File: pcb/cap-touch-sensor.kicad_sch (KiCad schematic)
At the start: 6 parts, among them U4 CAP1296-x-AIA

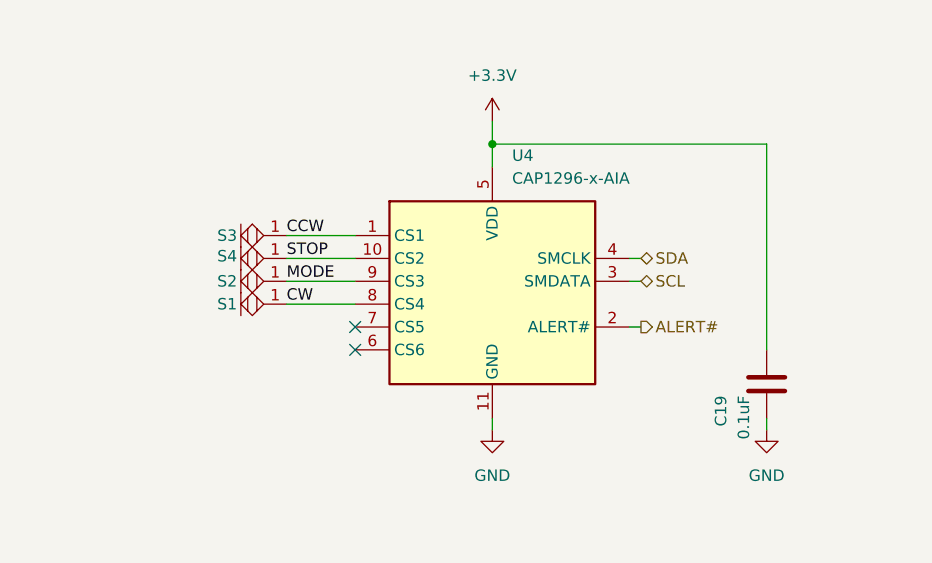
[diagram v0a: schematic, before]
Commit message: Revision E
- Resolve issues 1-11
- Add pdf of rev d schematic for easy comparison
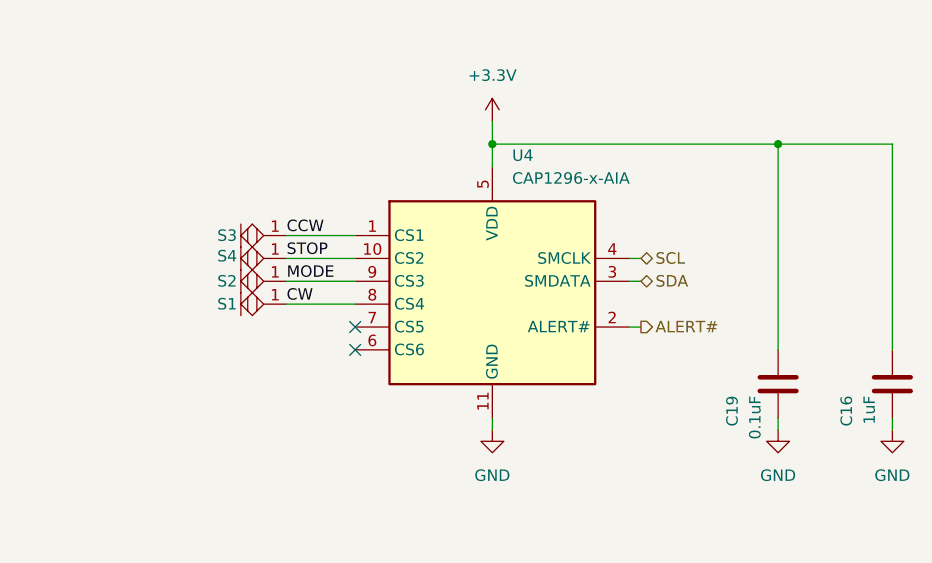
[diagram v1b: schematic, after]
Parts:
- added C16: 1uF, Capacitor_SMD:C_0603_1608Metric, symbol Device:C
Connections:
- net +3.3V: now also C16.1
- net GND: now also C16.2
- net SCL: now also U4.4 (SMCLK); no longer U4.3 (SMDATA)
- net SDA: now also U4.3 (SMDATA); no longer U4.4 (SMCLK)
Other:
- moved on the sheet: C19
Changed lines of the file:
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@@
+	)
+	(junction
+		(at 133.35 46.99)
+		(diameter 0)
+		(color 0 0 0 0)
 	)
 	(junction
@@
 	(wire
 		(pts
-			(xy 101.6 46.99) (xy 132.08 46.99)
+			(xy 101.6 46.99) (xy 133.35 46.99)
+		)
+		(stroke
+			(width 0)
+			(type default)
+		)
+	)
+	(wire
+		(pts
+			(xy 146.05 46.99) (xy 146.05 69.85)
 		)
 		(stroke
@@
 	(wire
 		(pts
-			(xy 132.08 46.99) (xy 132.08 69.85)
+			(xy 133.35 46.99) (xy 133.35 69.85)
 		)
 		(stroke
@@
 	(wire
 		(pts
+			(xy 133.35 46.99) (xy 146.05 46.99)
+		)
+		(stroke
+			(width 0)
+			(type default)
+		)
+	)
+	(wire
+		(pts
 			(xy 118.11 59.69) (xy 116.84 59.69)
 		)
@@
 	(wire
 		(pts
-			(xy 132.08 77.47) (xy 132.08 78.74)
+			(xy 133.35 77.47) (xy 133.35 78.74)
 		)
 		(stroke
@@
 		(pts
 			(xy 78.74 59.69) (xy 86.36 59.69)
+		)
+		(stroke
+			(width 0)
+			(type default)
+		)
+	)
+	(wire
+		(pts
+			(xy 146.05 77.47) (xy 146.05 78.74)
 		)
 		(stroke
@@
 	(hierarchical_label "SDA"
 		(shape bidirectional)
-		(at 118.11 59.69 0)
+		(at 118.11 62.23 0)
 		(fields_autoplaced yes)
 		(effects
@@
 	(hierarchical_label "SCL"
 		(shape bidirectional)
-		(at 118.11 62.23 0)
+		(at 118.11 59.69 0)
 		(fields_autoplaced yes)
 		(effects
@@
 	)
 	(symbol
+		(lib_id "power:GND")
+		(at 146.05 78.74 0)
+		(mirror y)
+		(unit 1)
+		(exclude_from_sim no)
+		(in_bom yes)
+		(on_board yes)
+		(dnp no)
+		(fields_autoplaced yes)
+		(property "Reference" "#PWR031"
+			(at 146.05 85.09 0)
+			(effects
+				(font
+					(size 1.27 1.27)
+				)
+				(hide yes)
+			)
+		)
+		(property "Value" "GND"
+			(at 146.05 83.82 0)
+			(effects
+				(font
+					(size 1.27 1.27)
+				)
+			)
+		)
+		(property "Footprint" ""
+			(at 146.05 78.74 0)
+			(effects
+				(font
+					(size 1.27 1.27)
+				)
+				(hide yes)
+			)
+		)
+		(property "Datasheet" ""
+			(at 146.05 78.74 0)
+			(effects
+				(font
+					(size 1.27 1.27)
+				)
+				(hide yes)
+			)
+		)
+		(property "Description" "Power symbol creates a global label with name \"GND\" , ground"
+			(at 146.05 78.74 0)
+			(effects
+				(font
+					(size 1.27 1.27)
+				)
+				(hide yes)
+			)
+		)
+		(pin "1"
+		)
+		(instances
+			(project "oe-commutator-controller"
+				(path "/f8e1d654-dc44-4fb2-953c-f5982945ff40/f9d22632-be45-4b30-a0f8-f307d3c7c772"
+					(reference "#PWR031")
+					(unit 1)
+				)
+			)
+		)
+	)
+	(symbol
 		(lib_id "Device:C")
-		(at 132.08 73.66 0)
+		(at 133.35 73.66 0)
 		(mirror y)
 		(unit 1)
@@
 		(dnp no)
 		(property "Reference" "C19"
-			(at 127 74.93 90)
+			(at 128.27 74.93 90)
 			(effects
 				(font
@@
 		)
 		(property "Value" "0.1uF"
-			(at 129.54 74.93 90)
+			(at 130.81 74.93 90)
 			(effects
 				(font
@@
 		)
 		(property "Footprint" "Capacitor_SMD:C_0402_1005Metric"
-			(at 131.1148 77.47 0)
+			(at 132.3848 77.47 0)
 			(effects
 				(font
@@
 		)
 		(property "Datasheet" "~"
-			(at 132.08 73.66 0)
+			(at 133.35 73.66 0)
 			(effects
 				(font
@@
 		)
 		(property "Description" "Unpolarized capacitor"
-			(at 132.08 73.66 0)
+			(at 133.35 73.66 0)
 			(effects
 				(font
@@
 				(path "/f8e1d654-dc44-4fb2-953c-f5982945ff40/f9d22632-be45-4b30-a0f8-f307d3c7c772"
 					(reference "C19")
+					(unit 1)
+				)
+			)
+		)
+	)
+	(symbol
+		(lib_id "Device:C")
+		(at 146.05 73.66 0)
+		(mirror y)
+		(unit 1)
+		(exclude_from_sim no)
+		(in_bom yes)
+		(on_board yes)
+		(dnp no)
+		(property "Reference" "C16"
+			(at 140.97 74.93 90)
+			(effects
+				(font
+					(size 1.27 1.27)
+				)
+				(justify right)
+			)
+		)
+		(property "Value" "1uF"
+			(at 143.51 74.93 90)
+			(effects
+				(font
+					(size 1.27 1.27)
+				)
+				(justify right)
+			)
+		)
+		(property "Footprint" "Capacitor_SMD:C_0603_1608Metric"
+			(at 145.0848 77.47 0)
+			(effects
+				(font
+					(size 1.27 1.27)
+				)
+				(hide yes)
+			)
+		)
+		(property "Datasheet" "~"
+			(at 146.05 73.66 0)
+			(effects
+				(font
+					(size 1.27 1.27)
+				)
+				(hide yes)
+			)
+		)
+		(property "Description" "Unpolarized capacitor"
+			(at 146.05 73.66 0)
+			(effects
+				(font
+					(size 1.27 1.27)
+				)
+				(hide yes)
+			)
+		)
+		(pin "1"
+		)
+		(pin "2"
+		)
+		(instances
+			(project "oe-commutator-controller"
+				(path "/f8e1d654-dc44-4fb2-953c-f5982945ff40/f9d22632-be45-4b30-a0f8-f307d3c7c772"
+					(reference "C16")
 					(unit 1)
 				)
@@
 	(symbol
 		(lib_id "power:GND")
-		(at 132.08 78.74 0)
+		(at 133.35 78.74 0)
 		(mirror y)
 		(unit 1)
@@
 		(fields_autoplaced yes)
 		(property "Reference" "#PWR037"
-			(at 132.08 85.09 0)
+			(at 133.35 85.09 0)
 			(effects
 				(font
@@
 		)
 		(property "Value" "GND"
-			(at 132.08 83.82 0)
+			(at 133.35 83.82 0)
 			(effects
 				(font
@@
 		)
 		(property "Footprint" ""
-			(at 132.08 78.74 0)
+			(at 133.35 78.74 0)
 			(effects
 				(font
@@
 		)
 		(property "Datasheet" ""
-			(at 132.08 78.74 0)
+			(at 133.35 78.74 0)
 			(effects
 				(font
@@
 		)
 		(property "Description" "Power symbol creates a global label with name \"GND\" , ground"
-			(at 132.08 78.74 0)
-			(effects
-				(font
+			(at 133.35 78.74 0)
+			(effects
+				(font

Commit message: Address schematic and PCB issues for Rev. E
- Some layout alternations
- Some schematic cleanup
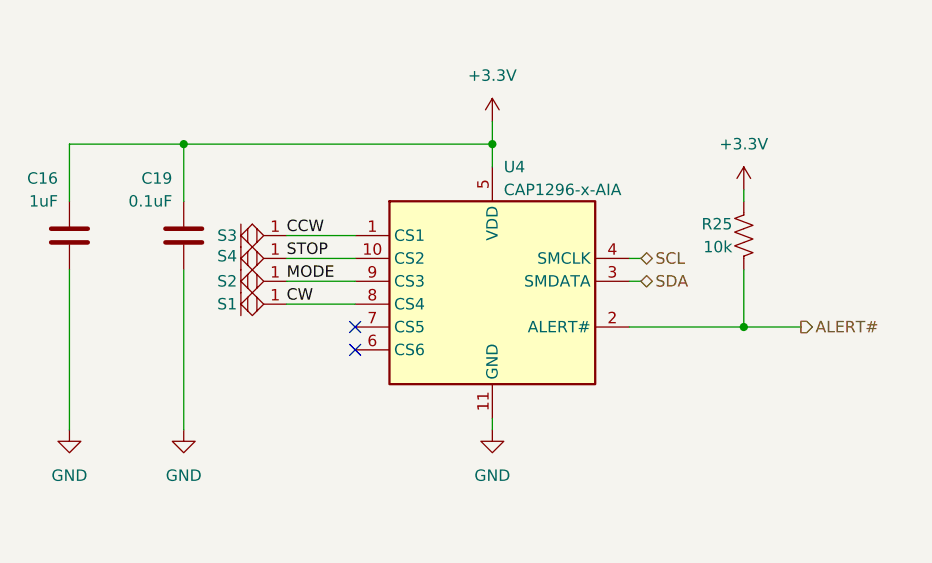
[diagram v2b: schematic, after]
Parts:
- added R25: 10k, Resistor_SMD:R_0603_1608Metric, symbol Device:R_US
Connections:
- net +3.3V: now also R25.1
- net ALERT#: now also R25.2
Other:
- moved on the sheet: C16, C19
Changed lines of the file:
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@@
 	(title_block
 		(title "Open Ephys Commutator Controller")
-		(rev "D")
+		(rev "E")
 		(company "Open Ephys, Inc.")
+		(comment 1 "Cris Sharp")
+		(comment 2 "Jonathan P. Newman")
 	)
 	(junction
-		(at 133.35 46.99)
+		(at 67.31 46.99)
+		(diameter 0)
+		(color 0 0 0 0)
+	)
+	(junction
+		(at 129.54 67.31)
 		(diameter 0)
 		(color 0 0 0 0)
@@
 	(wire
 		(pts
-			(xy 101.6 46.99) (xy 133.35 46.99)
-		)
-		(stroke
-			(width 0)
-			(type default)
-		)
-	)
-	(wire
-		(pts
-			(xy 146.05 46.99) (xy 146.05 69.85)
-		)
-		(stroke
-			(width 0)
-			(type default)
-		)
-	)
-	(wire
-		(pts
-			(xy 118.11 67.31) (xy 116.84 67.31)
+			(xy 67.31 46.99) (xy 101.6 46.99)
+		)
+		(stroke
+			(width 0)
+			(type default)
+		)
+	)
+	(wire
+		(pts
+			(xy 54.61 46.99) (xy 54.61 53.34)
+		)
+		(stroke
+			(width 0)
+			(type default)
+		)
+	)
+	(wire
+		(pts
+			(xy 135.89 67.31) (xy 129.54 67.31)
 		)
 		(stroke
@@
 	(wire
 		(pts
-			(xy 133.35 46.99) (xy 133.35 69.85)
+			(xy 67.31 46.99) (xy 67.31 53.34)
+		)
+		(stroke
+			(width 0)
+			(type default)
+		)
+	)
+	(wire
+		(pts
+			(xy 129.54 60.96) (xy 129.54 67.31)
 		)
 		(stroke
@@
 	(wire
 		(pts
+			(xy 129.54 52.07) (xy 129.54 53.34)
+		)
+		(stroke
+			(width 0)
+			(type default)
+		)
+	)
+	(wire
+		(pts
 			(xy 101.6 44.45) (xy 101.6 46.99)
 		)
@@
 	(wire
 		(pts
-			(xy 133.35 46.99) (xy 146.05 46.99)
+			(xy 67.31 46.99) (xy 54.61 46.99)
 		)
 		(stroke
@@
 	(wire
 		(pts
-			(xy 133.35 77.47) (xy 133.35 78.74)
+			(xy 67.31 60.96) (xy 67.31 78.74)
 		)
 		(stroke
@@
 	(wire
 		(pts
-			(xy 146.05 77.47) (xy 146.05 78.74)
+			(xy 54.61 60.96) (xy 54.61 78.74)
+		)
+		(stroke
+			(width 0)
+			(type default)
+		)
+	)
+	(wire
+		(pts
+			(xy 129.54 67.31) (xy 116.84 67.31)
 		)
 		(stroke
@@
 	(hierarchical_label "ALERT#"
 		(shape output)
-		(at 118.11 67.31 0)
+		(at 135.89 67.31 0)
 		(fields_autoplaced yes)
 		(effects
@@
 	(symbol
 		(lib_id "power:GND")
-		(at 146.05 78.74 0)
-		(mirror y)
+		(at 54.61 78.74 0)
 		(unit 1)
 		(exclude_from_sim no)
@@
 		(fields_autoplaced yes)
 		(property "Reference" "#PWR031"
-			(at 146.05 85.09 0)
+			(at 54.61 85.09 0)
 			(effects
 				(font
@@
 		)
 		(property "Value" "GND"
-			(at 146.05 83.82 0)
+			(at 54.61 83.82 0)
 			(effects
 				(font
@@
 		)
 		(property "Footprint" ""
-			(at 146.05 78.74 0)
+			(at 54.61 78.74 0)
 			(effects
 				(font
@@
 		)
 		(property "Datasheet" ""
-			(at 146.05 78.74 0)
+			(at 54.61 78.74 0)
 			(effects
 				(font
@@
 		)
 		(property "Description" "Power symbol creates a global label with name \"GND\" , ground"
-			(at 146.05 78.74 0)
+			(at 54.61 78.74 0)
 			(effects
 				(font
@@
 	)
 	(symbol
+		(lib_id "Device:R_US")
+		(at 129.54 57.15 0)
+		(mirror y)
+		(unit 1)
+		(exclude_from_sim no)
+		(in_bom yes)
+		(on_board yes)
+		(dnp no)
+		(property "Reference" "R25"
+			(at 128.27 55.88 0)
+			(effects
+				(font
+					(size 1.27 1.27)
+				)
+				(justify left)
+			)
+		)
+		(property "Value" "10k"
+			(at 128.27 58.42 0)
+			(effects
+				(font
+					(size 1.27 1.27)
+				)
+				(justify left)
+			)
+		)
+		(property "Footprint" "Resistor_SMD:R_0603_1608Metric"
+			(at 128.524 57.404 90)
+			(effects
+				(font
+					(size 1.27 1.27)
+				)
+				(hide yes)
+			)
+		)
+		(property "Datasheet" "~"
+			(at 129.54 57.15 0)
+			(effects
+				(font
+					(size 1.27 1.27)
+				)
+				(hide yes)
+			)
+		)
+		(property "Description" "Resistor, US symbol"
+			(at 129.54 57.15 0)
+			(effects
+				(font
+					(size 1.27 1.27)
+				)
+				(hide yes)
+			)
+		)
+		(pin "1"
+		)
+		(pin "2"
+		)
+		(instances
+			(project "oe-commutator-controller"
+				(path "/f8e1d654-dc44-4fb2-953c-f5982945ff40/f9d22632-be45-4b30-a0f8-f307d3c7c772"
+					(reference "R25")
+					(unit 1)
+				)
+			)
+		)
+	)
+	(symbol
 		(lib_id "Device:C")
-		(at 133.35 73.66 0)
-		(mirror y)
+		(at 67.31 57.15 0)
 		(unit 1)
 		(exclude_from_sim no)
@@
 		(dnp no)
 		(property "Reference" "C19"
-			(at 128.27 74.93 90)
+			(at 66.04 50.8 0)
 			(effects
 				(font
@@
 		)
 		(property "Value" "0.1uF"
-			(at 130.81 74.93 90)
+			(at 66.04 53.34 0)
 			(effects
 				(font
@@
 		)
 		(property "Footprint" "Capacitor_SMD:C_0402_1005Metric"
-			(at 132.3848 77.47 0)
+			(at 68.2752 60.96 0)
 			(effects
 				(font
@@
 		)
 		(property "Datasheet" "~"
-			(at 133.35 73.66 0)
+			(at 67.31 57.15 0)
 			(effects
 				(font
@@
 		)
 		(property "Description" "Unpolarized capacitor"
-			(at 133.35 73.66 0)
+			(at 67.31 57.15 0)
 			(effects
 				(font
@@
 	)
 	(symbol
+		(lib_id "power:+3.3V")
+		(at 129.54 52.07 0)
+		(unit 1)
+		(exclude_from_sim no)
+		(in_bom yes)
+		(on_board yes)
+		(dnp no)
+		(fields_autoplaced yes)
+		(property "Reference" "#PWR029"
+			(at 129.54 55.88 0)
+			(effects
+				(font
+					(size 1.27 1.27)
+				)
+				(hide yes)
+			)
+		)
+		(property "Value" "+3.3V"
+			(at 129.54 46.99 0)
+			(effects
+				(font
+					(size 1.27 1.27)
+				)
+			)
+		)
+		(property "Footprint" ""
+			(at 129.54 52.07 0)
+			(effects
+				(font
+					(size 1.27 1.27)
+				)
+				(hide yes)
+			)
+		)
+		(property "Datasheet" ""
+			(at 129.54 52.07 0)
+			(effects
+				(font
+					(size 1.27 1.27)
+				)
+				(hide yes)
+			)
+		)
+		(property "Description" "Power symbol creates a global label with name \"+3.3V\""
+			(at 129.54 52.07 0)
+			(effects
+				(font
+					(size 1.27 1.27)
+				)
+				(hide yes)
+			)
+		)
+		(pin "1"
+		)
+		(instances
+			(project "oe-commutator-controller"
+				(path "/f8e1d654-dc44-4fb2-953c-f5982945ff40/f9d22632-be45-4b30-a0f8-f307d3c7c772"
+					(reference "#PWR029")
+					(unit 1)
+				)
+			)
+		)
+	)
+	(symbol
 		(lib_id "Device:C")
-		(at 146.05 73.66 0)
-		(mirror y)
+		(at 54.61 57.15 0)
 		(unit 1)
 		(exclude_from_sim no)
@@
 		(dnp no)
 		(property "Reference" "C16"
-			(at 140.97 74.93 90)
+			(at 53.34 50.8 0)
 			(effects
 				(font
@@
 		)
 		(property "Value" "1uF"
-			(at 143.51 74.93 90)
+			(at 53.34 53.34 0)
 			(effects
 				(font
@@
 		)
 		(property "Footprint" "Capacitor_SMD:C_0603_1608Metric"
-			(at 145.0848 77.47 0)
+			(at 55.5752 60.96 0)
 			(effects
 				(font
@@
 		)
 		(property "Datasheet" "~"
-			(at 146.05 73.66 0)
+			(at 54.61 57.15 0)
 			(effects
 				(font
@@
 		)
 		(property "Description" "Unpolarized capacitor"
-			(at 146.05 73.66 0)
+			(at 54.61 57.15 0)
 			(effects
 				(font
@@
 	(symbol
 		(lib_id "power:GND")
-		(at 133.35 78.74 0)
-		(mirror y)
+		(at 67.31 78.74 0)
 		(unit 1)
 		(exclude_from_sim no)
@@
 		(fields_autoplaced yes)
 		(property "Reference" "#PWR037"
-			(at 133.35 85.09 0)
+			(at 67.31 85.09 0)
 			(effects
 				(font
@@
 		)
 		(property "Value" "GND"
-			(at 133.35 83.82 0)
+			(at 67.31 83.82 0)
 			(effects
 				(font
@@
 		)
 		(property "Footprint" ""
-			(at 133.35 78.74 0)
+			(at 67.31 78.74 0)
 			(effects
 				(font
@@
 		)
 		(property "Datasheet" ""
-			(at 133.35 78.74 0)
+			(at 67.31 78.74 0)
 			(effects
 				(font
@@
 		)
 		(property "Description" "Power symbol creates a global label with name \"GND\" , ground"
-			(at 133.35 78.74 0)
+			(at 67.31 78.74 0)
 			(effects
 				(font
@@
 		(on_board yes)
 		(dnp no)
-		(fields_autoplaced yes)
 		(property "Reference" "U4"
-			(at 103.7941 48.26 0)
+			(at 102.87 49.53 0)
 			(effects
 				(font
@@
 		)
 		(property "Value" "CAP1296-x-AIA"
-			(at 103.7941 50.8 0)
-			(effects
-				(font
+			(at 102.87 52.07 0)
+			(effects
+				(font

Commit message: Revision F Edits
- Reduce base capacitance
  - Reduce infill {width, gap}: {0.35, 1} -> {0.2, 1.2}
    - Equivalent to: 45.1% -> 26.5%
  - Entirely remove copper on 3rd (in2.Cu) layer
  - Reduce via count
- export rev e schematic to pdf
- put pdfs into manufacturing folder
- Fix 6mm tactile switch footprint
- Put gold under logo
- Increment schematic, pcb, and silkscreen revision to F
- Add labels to debug header
- Add 10k pull-up to tmc2130 enable pin
- Convert all symbols & footprints library aliases from "oe" to "open-ephys"
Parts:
- S1, S2, S3, S4: footprint oe:Touch_Center_2mm -> open-ephys:Touch_Center_2mm; symbol oe:TOUCH -> open-ephys:TOUCH; now left out of the parts list
- U4: symbol oe:CAP1296-x-AIA -> open-ephys:CAP1296-x-AIA
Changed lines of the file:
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@@
 	)
 	(symbol
-		(lib_id "oe:TOUCH")
+		(lib_id "open-ephys:TOUCH")
 		(at 76.2 59.69 90)
 		(mirror x)
 		(unit 1)
 		(exclude_from_sim no)
-		(in_bom yes)
+		(in_bom no)
 		(on_board yes)
 		(dnp no)
@@
 			)
 		)
-		(property "Footprint" "oe:Touch_Center_2mm"
+		(property "Footprint" "open-ephys:Touch_Center_2mm"
 			(at 76.2 59.69 0)
 			(effects
@@
 			)
 		)
-		(property "Description" ""
+		(property "Description" "Printed capactitive touch sensor"
 			(at 76.2 59.69 0)
 			(effects
@@
 	)
 	(symbol
-		(lib_id "oe:TOUCH")
+		(lib_id "open-ephys:TOUCH")
 		(at 76.2 62.23 90)
 		(mirror x)
 		(unit 1)
 		(exclude_from_sim no)
-		(in_bom yes)
+		(in_bom no)
 		(on_board yes)
 		(dnp no)
@@
 			)
 		)
-		(property "Footprint" "oe:Touch_Center_2mm"
+		(property "Footprint" "open-ephys:Touch_Center_2mm"
 			(at 76.2 62.23 0)
 			(effects
@@
 			)
 		)
-		(property "Description" ""
+		(property "Description" "Printed capactitive touch sensor"
 			(at 76.2 62.23 0)
 			(effects
@@
 	)
 	(symbol
-		(lib_id "oe:TOUCH")
+		(lib_id "open-ephys:TOUCH")
 		(at 76.2 57.15 90)
 		(mirror x)
 		(unit 1)
 		(exclude_from_sim no)
-		(in_bom yes)
+		(in_bom no)
 		(on_board yes)
 		(dnp no)
@@
 			)
 		)
-		(property "Footprint" "oe:Touch_Center_2mm"
+		(property "Footprint" "open-ephys:Touch_Center_2mm"
 			(at 76.2 57.15 0)
 			(effects
@@
 			)
 		)
-		(property "Description" ""
+		(property "Description" "Printed capactitive touch sensor"
 			(at 76.2 57.15 0)
 			(effects
@@
 	)
 	(symbol
-		(lib_id "oe:CAP1296-x-AIA")
+		(lib_id "open-ephys:CAP1296-x-AIA")
 		(at 101.6 64.77 0)
 		(unit 1)
@@
 	)
 	(symbol
-		(lib_id "oe:TOUCH")
+		(lib_id "open-ephys:TOUCH")
 		(at 76.2 64.77 90)
 		(mirror x)
 		(unit 1)
 		(exclude_from_sim no)
-		(in_bom yes)
+		(in_bom no)
 		(on_board yes)
 		(dnp no)
@@
 			)
 		)
-		(property "Footprint" "oe:Touch_Center_2mm"
+		(property "Footprint" "open-ephys:Touch_Center_2mm"
 			(at 76.2 64.77 0)
 			(effects
@@
 			)
 		)
-		(property "Description" ""
+		(property "Description" "Printed capactitive touch sensor"
 			(at 76.2 64.77 0)
 			(effects

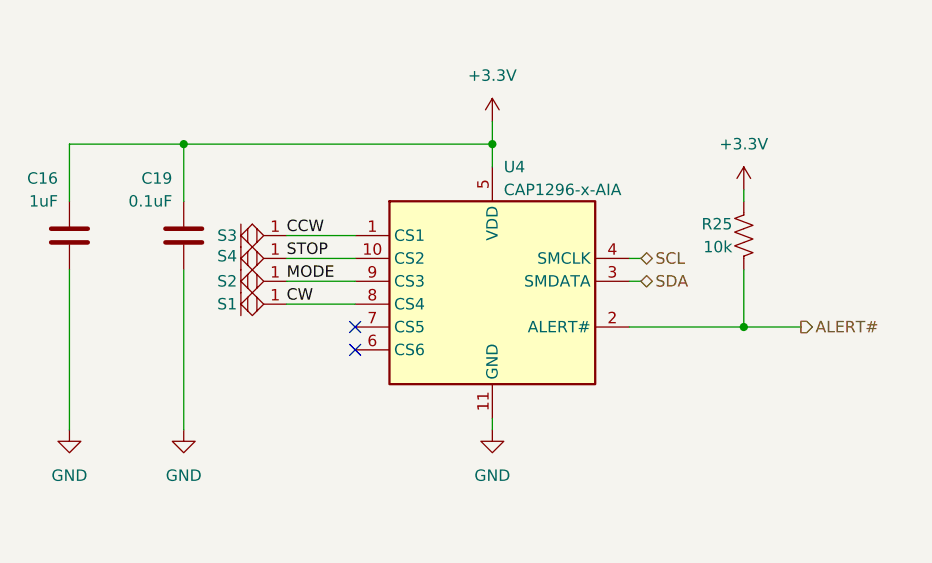
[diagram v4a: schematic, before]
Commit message: Add caps in series with touch sensor
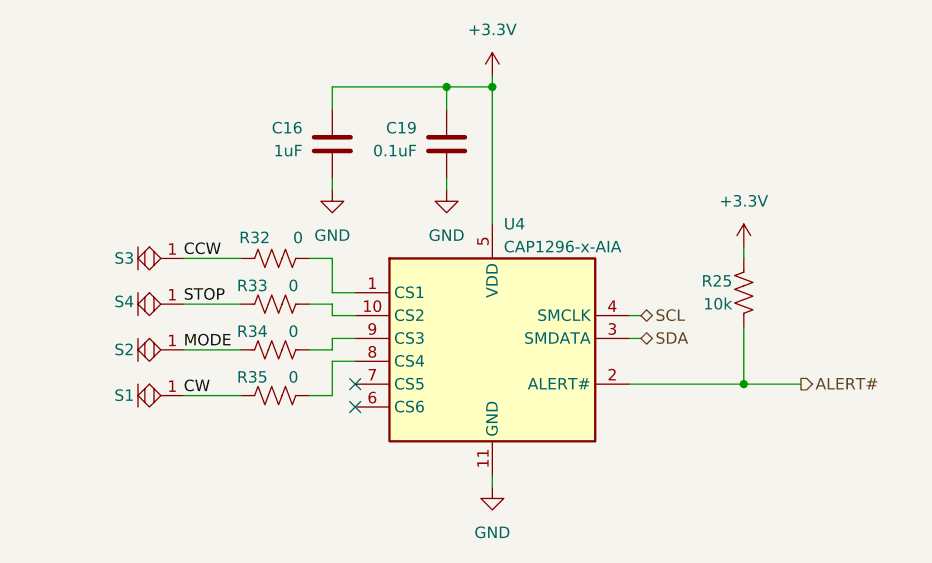
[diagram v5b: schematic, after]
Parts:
- added R32, R33, R34, R35: 0, Resistor_SMD:R_0402_1005Metric, symbol Device:R_US
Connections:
- net CCW: now also R32.1; no longer U4.1 (CS1)
- net CW: now also R35.1; no longer U4.8 (CS4)
- net MODE: now also R34.1; no longer U4.9 (CS3)
- net STOP: now also R33.1; no longer U4.10 (CS2)
- new net: R32.2, U4.1 (CS1)
- new net: R35.2, U4.8 (CS4)
- new net: R34.2, U4.9 (CS3)
- new net: R33.2, U4.10 (CS2)
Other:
- moved on the sheet: C16, C19, R25, S1, S2, S3, S4, U4
